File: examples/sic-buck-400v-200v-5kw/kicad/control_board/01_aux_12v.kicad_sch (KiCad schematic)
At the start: 15 parts, among them J1 12 V in, U1 TPS26400PWPR

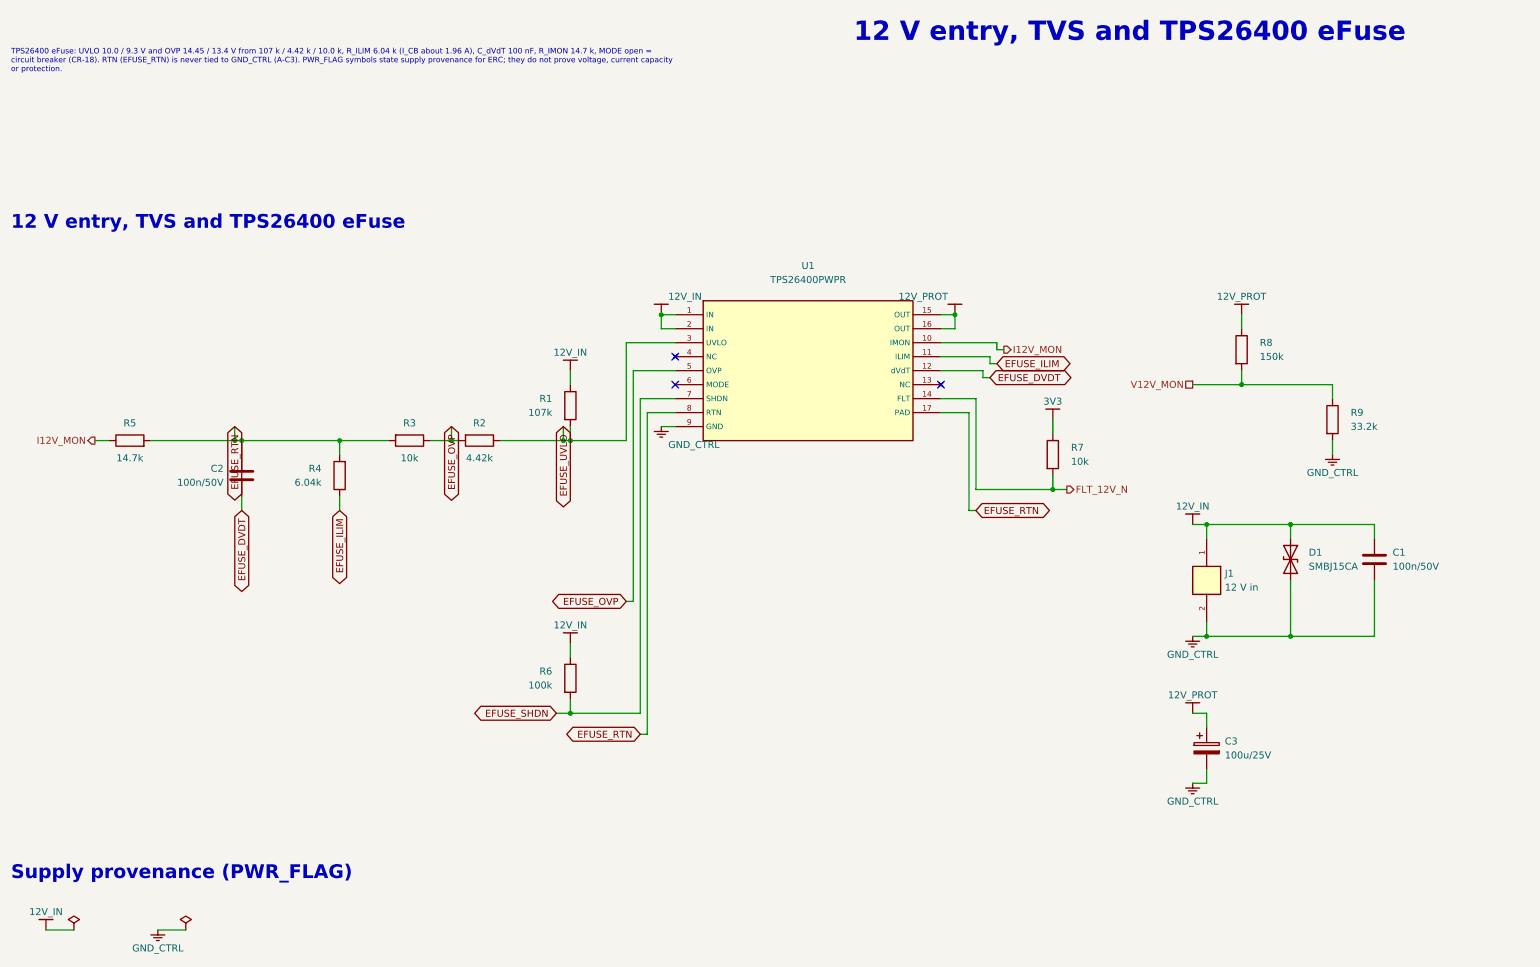
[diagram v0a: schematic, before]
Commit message: Correct sensing circuits and add verified V2.2 local bypasses
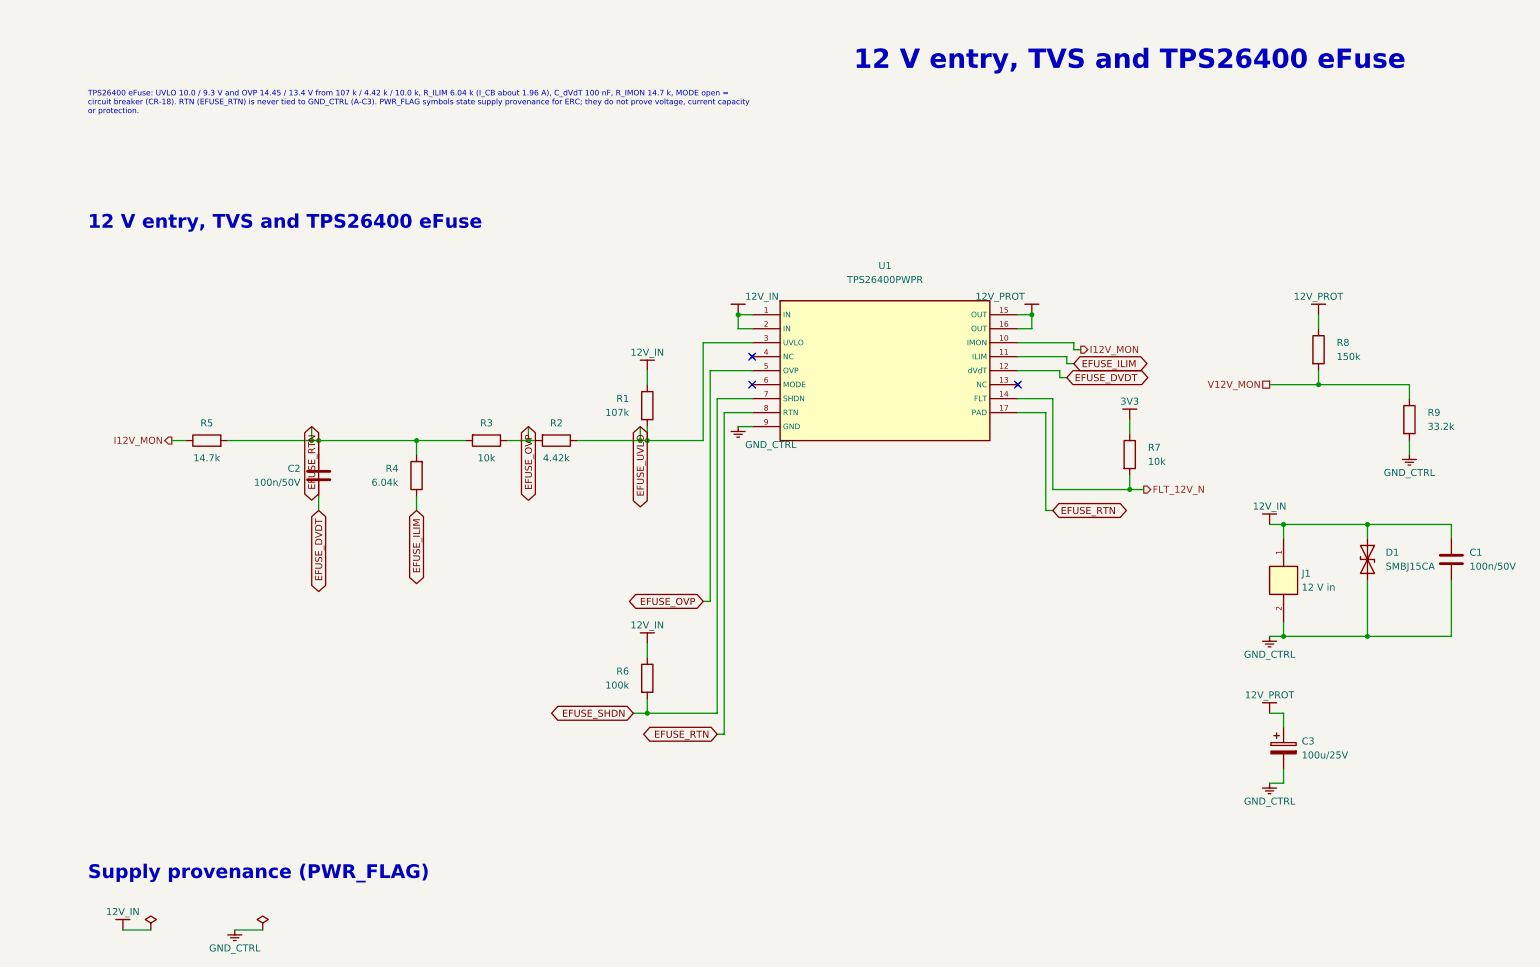
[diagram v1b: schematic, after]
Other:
- moved on the sheet: C1, C2, C3, D1, J1, R1, R2, R3, R4, R5, R6, R7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
